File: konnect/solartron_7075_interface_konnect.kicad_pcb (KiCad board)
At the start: 2 copper layers, 74 x 74 mm, 93 parts, among them J1 DD-50 Male (Solartron SKB), J2 USB_B, J3 SWD, Q1 2N7002, SW1 BOOTSEL, SW2 RUN, U1 RP2354A, U11 AMS1117-3.3, U12 SN74LVC165APWR, U13 SN74LVC165APWR, U14 SN74LVC165APWR, U15 SN74LVC165APWR, U16 SN74LVC165APWR, U17 74LVC595APW, U18 74LVC595APW, U19 74LVC1G17, U2 USBLC6-2SC6, U3 AP2112K-3.3, U4 TLP2361, U5 TLP2361, U6 TLP2361, U7 TLP2361, U8 TLP2361, U9 TLP2361, Y1 12MHz

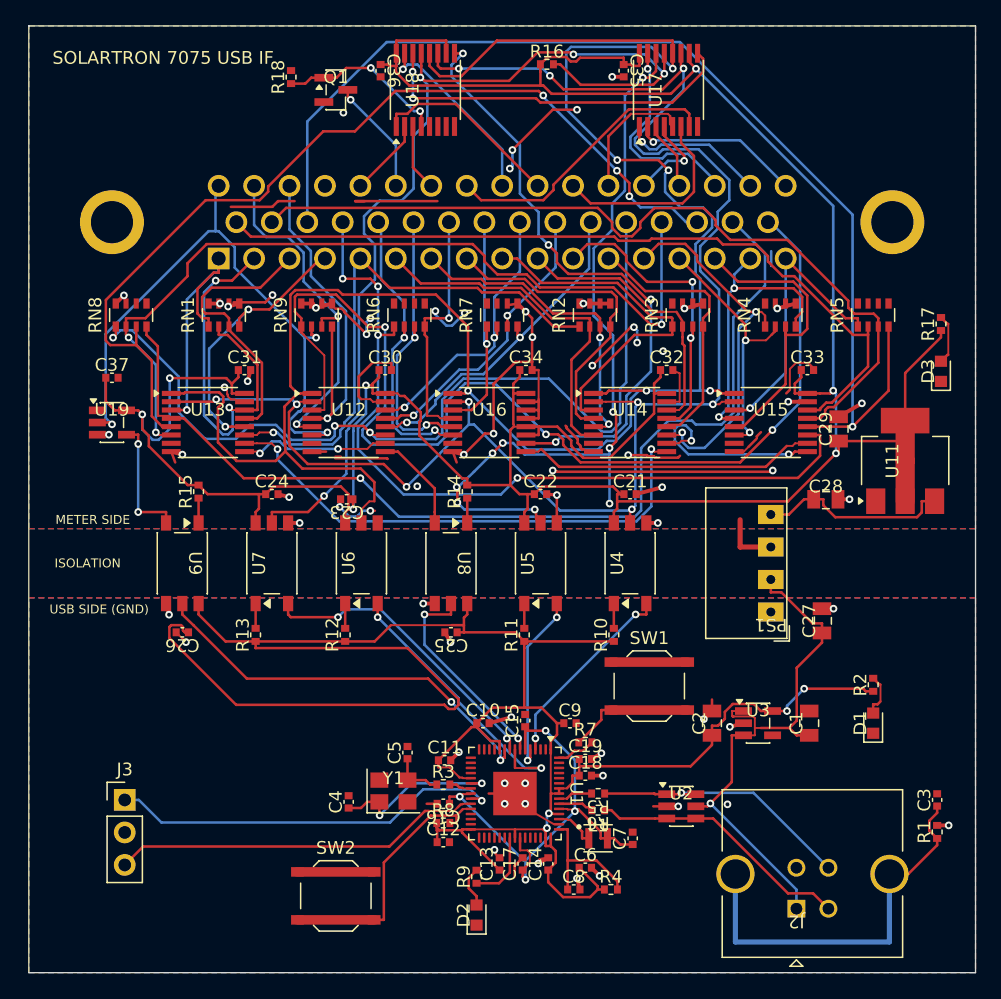
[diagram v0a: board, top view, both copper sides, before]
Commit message: Konnect: pin-swap the shift registers and resistor arrays, re-route meter side
- Re-assigned the 36 DVM inputs across the five '165s and nine 100k arrays,
  within and between identical parts, so each array feeds one side of one
  '165 in D-sub pin order. Reordered the '595 outputs to match the D-sub
  top row. U16 keeps its 0,0,1,1 signature; the schematic note now carries
  the full MISO/MOSI bit map (SAMPLE moved to U18 QA/QC).
- Pre-placed the '165 LOAD/SCK escapes and bottom-layer buses, and ground
  pockets for the arrays and the '165 GND/CLK INH pins, then re-routed the
  meter side with Freerouting. The USB side is unchanged.
- Meter-side signals: 2,374 mm / 111 vias -> 1,692 mm / 55 vias; the 36
  input nets alone: 1,343 mm / 53 vias -> 781 mm / 7 vias.
- ERC clean. DRC: 0 unconnected, 4 cosmetic starved-thermal errors
  (C17, C24, C30, C31). Fab outputs regenerated; BOM and positions unchanged.

Co-Authored-By: Claude Opus 5.5 <noreply@anthropic.com>
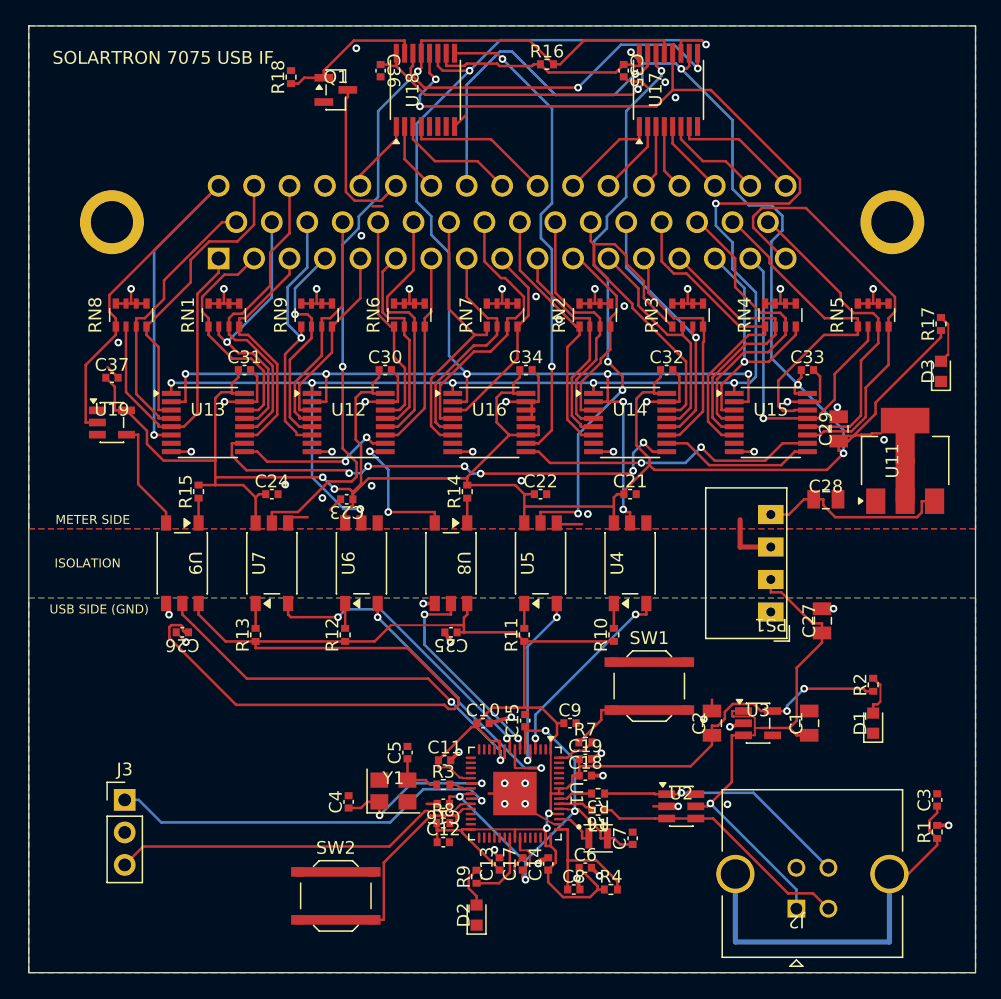
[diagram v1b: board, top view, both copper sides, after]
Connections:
- RN1 pad 1: /BCD6_1 -> /BCD5_8
- RN1 pad 2: /BCD5_8 -> /BCD1_4
- RN1 pad 3: /BCD5_4 -> /OVERLOAD
- RN1 pad 4: /BCD5_2 -> /BCD5_4
- RN2 pad 1: /BCD5_1 -> /POL_POS
- RN2 pad 2: /BCD4_8 -> /BCD3_8
- RN2 pad 3: /BCD4_4 -> /POL_NEG
- RN2 pad 4: /BCD4_2 -> /BCD3_4
- RN3 pad 1: /BCD4_1 -> /FN_OUT_28
- RN3 pad 2: /BCD3_8 -> /BCD3_2
- RN3 pad 3: /BCD3_4 -> /FN_OUT_29
- RN3 pad 4: /BCD3_2 -> /BCD3_1
- RN4 pad 1: /BCD3_1 -> /RNG_OUT_4
- RN4 pad 3: /BCD2_4 -> /RNG_OUT_2
- RN4 pad 4: /BCD2_2 -> /BCD2_4
- RN5 pad 1: /BCD2_1 -> /RNG_OUT_1
- RN5 pad 2: /BCD1_8 -> /BCD2_2
- RN5 pad 3: /BCD1_4 -> /PRINT_PULSE
- RN5 pad 4: /BCD1_2 -> /BCD2_1
- RN6 pad 1: /BCD1_1 -> /BCD0_8
- RN6 pad 2: /BCD0_8 -> /BCD4_8
- RN6 pad 4: /BCD0_2 -> /BCD4_4
- RN7 pad 1: /BCD0_1 -> /BCD0_2
- RN7 pad 2: /POL_POS -> /BCD4_2
- RN7 pad 3: /POL_NEG -> /BCD0_1
- RN7 pad 4: /FN_OUT_28 -> /BCD4_1
- RN8 pad 1: /FN_OUT_29 -> /PRINT_LEVEL
- RN8 pad 2: /RNG_OUT_4 -> /BCD6_1
- RN8 pad 3: /RNG_OUT_2 -> /BCD1_8
- RN8 pad 4: /RNG_OUT_1 -> /DATA_CAN_CHANGE
- RN9 pad 1: /PRINT_PULSE -> /BCD1_2
- RN9 pad 2: /PRINT_LEVEL -> /BCD5_2
- RN9 pad 3: /DATA_CAN_CHANGE -> /BCD1_1
- RN9 pad 4: /OVERLOAD -> /BCD5_1
- U12 pad 11: /FN_OUT_29 -> /BCD4_4
- U12 pad 12: /FN_OUT_28 -> /BCD0_4
- U12 pad 13: /POL_NEG -> /BCD4_8
- U12 pad 14: /POL_POS -> /BCD0_8
- U12 pad 3: /PRINT_PULSE -> /BCD5_1
- U12 pad 4: /OVERLOAD -> /BCD1_1
- U12 pad 5: /DATA_CAN_CHANGE -> /BCD5_2
- U12 pad 6: /PRINT_LEVEL -> /BCD1_2
- U13 pad 11: /BCD5_1 -> /BCD5_4
- U13 pad 12: /BCD5_2 -> /OVERLOAD
- U13 pad 13: /BCD5_4 -> /BCD1_4
- U13 pad 3: /BCD6_1 -> /DATA_CAN_CHANGE
- U13 pad 4: /RNG_OUT_1 -> /BCD1_8
- U13 pad 5: /RNG_OUT_2 -> /BCD6_1
- U13 pad 6: /RNG_OUT_4 -> /PRINT_LEVEL
- U14 pad 12: /BCD3_2 -> /FN_OUT_29
- U14 pad 13: /BCD3_4 -> /BCD3_2
- U14 pad 14: /BCD3_8 -> /FN_OUT_28
- U14 pad 3: /BCD4_1 -> /BCD3_4
- U14 pad 4: /BCD4_2 -> /POL_NEG
- U14 pad 5: /BCD4_4 -> /BCD3_8
- U14 pad 6: /BCD4_8 -> /POL_POS
- U15 pad 11: /BCD1_1 -> /BCD2_1
- U15 pad 12: /BCD1_2 -> /PRINT_PULSE
- U15 pad 13: /BCD1_4 -> /BCD2_2
- U15 pad 14: /BCD1_8 -> /RNG_OUT_1
- U15 pad 3: /BCD2_1 -> /BCD2_4
- U15 pad 4: /BCD2_2 -> /RNG_OUT_2
- U15 pad 5: /BCD2_4 -> /BCD2_8
- U15 pad 6: /BCD2_8 -> /RNG_OUT_4
- U16 pad 3: /BCD0_1 -> /BCD4_1
- U16 pad 4: /BCD0_2 -> /BCD0_1
- U16 pad 5: /BCD0_4 -> /BCD4_2
- U16 pad 6: /BCD0_8 -> /BCD0_2
- U17 pad 1: /CMD_RNG_2 -> /CMD_INT_4
- U17 pad 15: /CMD_RNG_1 -> /CMD_RATIO_N
- U17 pad 2: /CMD_RNG_4 -> /CMD_INT_2
- U17 pad 3: /CMD_AUTORANGE_INH -> /CMD_INT_1
- U17 pad 4: /CMD_INT_1 -> /CMD_AUTORANGE_INH
- U17 pad 5: /CMD_INT_2 -> /CMD_RNG_1
- U17 pad 6: /CMD_INT_4 -> /CMD_RNG_2
- U17 pad 7: /CMD_RATIO_N -> /CMD_RNG_4
- U18 pad 1: /CMD_FN_43 -> /CMD_FPL_N
- U18 pad 15: /CMD_FN_42 -> /SAMPLE_CONTACT_DRV
- U18 pad 2: /CMD_FPL_N -> /CMD_SAMPLE_PULSE
- U18 pad 3: /CMD_SAMPLE_PULSE -> /CMD_FN_42
- U18 pad 4: /SAMPLE_CONTACT_DRV -> /CMD_FN_43
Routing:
- net GND_ISO: track 154.4 -> 81.4 mm, vias 43 -> 34
- net /BCD1_2: track 87.7 -> 20.7 mm
- net /PRINT_PULSE: track 86.2 -> 24.8 mm, vias 3 -> 0
- net /RNG_OUT_1: track 79.1 -> 26.6 mm, vias 1 -> 0
- net /FN_OUT_29: track 70.9 -> 20.8 mm, vias 3 -> 1
- net /RNG_OUT_2: track 73.2 -> 23.6 mm, vias 3 -> 0
- net /BCD1_1: track 64.2 -> 18.4 mm, vias 4 -> 0
- net /BCD1_4: track 65.3 -> 21.7 mm, vias 0 -> 1
- net /BCD1_8: track 62.7 -> 21.3 mm
- net /RNG_OUT_4: track 66.9 -> 25.8 mm, vias 3 -> 0
- net /ISO_LOAD: track 159.6 -> 127.0 mm, vias 6 -> 9
- net /BCD5_1: track 42.1 -> 14.8 mm, vias 1 -> 0
- net /ISO_MOSI: track 60.9 -> 44.6 mm, vias 9 -> 4
- net /BCD4_1: track 28.1 -> 15.8 mm
- net /BCD4_8: track 28.1 -> 15.9 mm
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
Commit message: Konnect: move the meter-side parts and lay out the input wiring by script
- U16 (four DVM inputs) moves to the right-hand end so the nine used '165
  input sides sit in a row at twice the D-sub group pitch; each array sits
  under its four D-sub pins, turned to face the connector. The 36 input
  tracks follow one repeated pattern: straight into the array, out between
  its pad rows, and into each '165 side from outside and from under the
  body. One via (DD-50 pin 36, which sits above pin 3).
- '165 decoupling caps moved onto the chips with a bottom-layer +3V3_ISO
  spine; C29 moved above the regulator; U19 turned to face U13.
- Both shift-register chains now run in board order (MOSI -> U18 -> U17 ->
  U16 -> U15 -> U14 -> U12 -> U13 -> MISO) and CMD_RATIO_N moves to U18 QD.
  The schematic note carries the new bit map.
- Control buses, supply rails, SIPO links and the '165 chain were also laid
  by script; Freerouting did the rest. USB side unchanged.
- Meter-side signals: 1,692 mm / 55 vias -> 1,558 mm / 36 vias; the 36
  input nets: 781 mm / 7 vias -> 655 mm / 1 via.
- ERC clean. DRC: 0 unconnected, one cosmetic starved thermal (C17, as in
  the first layout). Fab outputs and positions regenerated; BOM unchanged.

Co-Authored-By: Claude Opus 5.5 <noreply@anthropic.com>
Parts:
- moved C34 23.9 mm to (162.7, 126.9), turned to 90 degrees
- moved U16 23.9 mm to (159.9, 131.0)
- moved U14 9.31 mm to (137.7, 131.0)
- moved C32 9.30 mm to (140.6, 126.9), turned to 90 degrees
- moved U15 9.23 mm to (148.8, 131.0)
- moved C33 9.22 mm to (151.6, 126.9), turned to 90 degrees
- moved RN5 8.92 mm to (157.1, 122.6), turned to -90 degrees
- moved RN4 7.21 mm to (151.5, 122.6), turned to -90 degrees
- moved C37 6.50 mm to (106.5, 134.0)
- moved RN3 5.50 mm to (146.0, 122.6), turned to -90 degrees
- moved C29 5.38 mm to (167.0, 127.6), turned to 0 degrees
- moved RN8 4.76 mm to (112.8, 122.6), turned to -90 degrees
- moved RN2 3.79 mm to (140.5, 122.6), turned to -90 degrees
- moved RN1 3.05 mm to (118.3, 122.6), turned to -90 degrees
- moved RN7 2.08 mm to (134.9, 122.6), turned to -90 degrees
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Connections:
- RN1 pad 1: /BCD5_8 -> /BCD5_4
- RN1 pad 2: /BCD1_4 -> /OVERLOAD
- RN1 pad 3: /OVERLOAD -> /BCD1_4
- RN1 pad 4: /BCD5_4 -> /BCD5_8
- RN2 pad 1: /POL_POS -> /BCD3_4
- RN2 pad 2: /BCD3_8 -> /POL_NEG
- RN2 pad 3: /POL_NEG -> /BCD3_8
- RN2 pad 4: /BCD3_4 -> /POL_POS
- RN3 pad 1: /FN_OUT_28 -> /BCD3_1
- RN3 pad 2: /BCD3_2 -> /FN_OUT_29
- RN3 pad 3: /FN_OUT_29 -> /BCD3_2
- RN3 pad 4: /BCD3_1 -> /FN_OUT_28
- RN4 pad 1: /RNG_OUT_4 -> /BCD2_4
- RN4 pad 2: /BCD2_8 -> /RNG_OUT_2
- RN4 pad 3: /RNG_OUT_2 -> /BCD2_8
- RN4 pad 4: /BCD2_4 -> /RNG_OUT_4
- RN5 pad 1: /RNG_OUT_1 -> /BCD2_1
- RN5 pad 2: /BCD2_2 -> /PRINT_PULSE
- RN5 pad 3: /PRINT_PULSE -> /BCD2_2
- RN5 pad 4: /BCD2_1 -> /RNG_OUT_1
- RN6 pad 1: /BCD0_8 -> /BCD4_4
- RN6 pad 2: /BCD4_8 -> /BCD0_4
- RN6 pad 3: /BCD0_4 -> /BCD4_8
- RN6 pad 4: /BCD4_4 -> /BCD0_8
- RN7 pad 1: /BCD0_2 -> /BCD4_1
- RN7 pad 2: /BCD4_2 -> /BCD0_1
- RN7 pad 3: /BCD0_1 -> /BCD4_2
- RN7 pad 4: /BCD4_1 -> /BCD0_2
- RN8 pad 1: /PRINT_LEVEL -> /BCD6_1
- RN8 pad 2: /BCD6_1 -> /DATA_CAN_CHANGE
- RN8 pad 4: /DATA_CAN_CHANGE -> /PRINT_LEVEL
- RN9 pad 1: /BCD1_2 -> /BCD5_1
- RN9 pad 2: /BCD5_2 -> /BCD1_1
- RN9 pad 3: /BCD1_1 -> /BCD5_2
- RN9 pad 4: /BCD5_1 -> /BCD1_2
- U12 pad 10: /PISO_CH1 -> /PISO_CH2
- U12 pad 11: /BCD4_4 -> /BCD0_8
- U12 pad 12: /BCD0_4 -> /BCD4_8
- U12 pad 13: /BCD4_8 -> /BCD4_4
- U12 pad 14: /BCD0_8 -> /BCD0_4
- U12 pad 3: /BCD5_1 -> /BCD5_2
- U12 pad 4: /BCD1_1 -> /BCD1_2
- U12 pad 5: /BCD5_2 -> /BCD1_1
- U12 pad 6: /BCD1_2 -> /BCD5_1
- U12 pad 9: /ISO_MISO -> /PISO_CH1
- U13 pad 10: /PISO_CH2 -> /PISO_CH1
- U13 pad 11: /BCD5_4 -> /BCD5_8
- U13 pad 12: /OVERLOAD -> /BCD1_4
- U13 pad 13: /BCD1_4 -> /BCD5_4
- U13 pad 14: /BCD5_8 -> /OVERLOAD
- U13 pad 3: /DATA_CAN_CHANGE -> /BCD1_8
- U13 pad 4: /BCD1_8 -> /PRINT_LEVEL
- U13 pad 5: /BCD6_1 -> /DATA_CAN_CHANGE
- U13 pad 6: /PRINT_LEVEL -> /BCD6_1
- U13 pad 9: /PISO_CH1 -> /ISO_MISO
- U14 pad 11: /BCD3_1 -> /POL_POS
- U14 pad 12: /FN_OUT_29 -> /BCD3_8
- U14 pad 13: /BCD3_2 -> /BCD3_4
- U14 pad 14: /FN_OUT_28 -> /POL_NEG
- U14 pad 3: /BCD3_4 -> /BCD4_2
- U14 pad 4: /POL_NEG -> /BCD0_2
- U14 pad 5: /BCD3_8 -> /BCD0_1
- U14 pad 6: /POL_POS -> /BCD4_1
- U15 pad 11: /BCD2_1 -> /RNG_OUT_4
- U15 pad 12: /PRINT_PULSE -> /BCD2_8
- U15 pad 13: /BCD2_2 -> /BCD2_4
- U15 pad 14: /RNG_OUT_1 -> /RNG_OUT_2
- U15 pad 3: /BCD2_4 -> /BCD3_2
- U15 pad 4: /RNG_OUT_2 -> /FN_OUT_28
- U15 pad 5: /BCD2_8 -> /FN_OUT_29
- U15 pad 6: /RNG_OUT_4 -> /BCD3_1
- U16 pad 3: /BCD4_1 -> /BCD2_2
- U16 pad 4: /BCD0_1 -> /RNG_OUT_1
- U16 pad 5: /BCD4_2 -> /PRINT_PULSE
- U16 pad 6: /BCD0_2 -> /BCD2_1
- U17 pad 14: /ISO_MOSI -> /SIPO_CH1
- U17 pad 15: /CMD_RATIO_N -> unconnected-(U17-QA-Pad15)
- U17 pad 9: /SIPO_CH1 -> /SIPO_LOOP
- U18 pad 14: /SIPO_CH1 -> /ISO_MOSI
- U18 pad 3: /CMD_FN_42 -> /CMD_RATIO_N
- U18 pad 4: /CMD_FN_43 -> /CMD_FN_42
- U18 pad 5: unconnected-(U18-QF-Pad5) -> /CMD_FN_43
- U18 pad 9: /SIPO_LOOP -> /SIPO_CH1
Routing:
- net /PISO_CH2: track 39.1 -> 15.5 mm, vias 6 -> 0
- net /PRINT_LEVEL: track 47.0 -> 25.8 mm, vias 1 -> 0
- net /ISO_OE_N: track 67.2 -> 87.5 mm, vias 2 -> 4
- net /CMD_RATIO_N: track 26.5 -> 6.71 mm, vias 1 -> 0
- net /ISO_LOAD: track 127.0 -> 145.3 mm, vias 9 -> 8
- net /BCD2_1: track 34.1 -> 17.3 mm
- net GND_ISO: track 81.4 -> 64.8 mm, vias 34 -> 27
- net /ISO_SCK: track 124.9 -> 112.6 mm, vias 9 -> 10
- net /BCD2_2: track 26.1 -> 15.0 mm, vias 1 -> 0
- net /FN_OUT_28: track 29.0 -> 18.6 mm
- net /SIPO_LOOP: track 37.7 -> 47.1 mm, vias 2 -> 0
- net /PISO_CH4: track 23.9 -> 15.5 mm, vias 2 -> 0
- net /RNG_OUT_1: track 26.6 -> 18.6 mm
- net /BCD6_1: track 25.1 -> 17.3 mm
- net /ISO_MISO: track 11.0 -> 18.9 mm, vias 2 -> 0
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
